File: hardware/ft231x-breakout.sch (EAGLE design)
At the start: 25 parts, among them Q1 2N7002PW, U1 FT231XS, X1 USB-MICROB

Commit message: Silkscreen fixes: no-silk headers, moved labels
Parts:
- JP1: device SparkFun-Connectors:M06SIP -> SparkFun-Connectors:M06SIP-NS
- JP10, JP11: device SparkFun-Connectors:M07 -> SparkFun-Connectors:M07NS
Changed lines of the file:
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@@
 <grid distance="0.1" unitdist="inch" unit="inch" style="lines" multiple="1" display="no" altdistance="0.01" altunitdist="inch" altunit="inch"/>
 <layers>
-<layer number="1" name="Top" color="4" fill="1" visible="no" active="no"/>
-<layer number="2" name="Route2" color="1" fill="3" visible="no" active="no"/>
-<layer number="3" name="Route3" color="4" fill="3" visible="no" active="no"/>
-<layer number="4" name="Route4" color="1" fill="4" visible="no" active="no"/>
-<layer number="5" name="Route5" color="4" fill="4" visible="no" active="no"/>
-<layer number="6" name="Route6" color="1" fill="8" visible="no" active="no"/>
-<layer number="7" name="Route7" color="4" fill="8" visible="no" active="no"/>
-<layer number="8" name="Route8" color="1" fill="2" visible="no" active="no"/>
-<layer number="9" name="Route9" color="4" fill="2" visible="no" active="no"/>
-<layer number="10" name="Route10" color="1" fill="7" visible="no" active="no"/>
-<layer number="11" name="Route11" color="4" fill="7" visible="no" active="no"/>
-<layer number="12" name="Route12" color="1" fill="5" visible="no" active="no"/>
-<layer number="13" name="Route13" color="4" fill="5" visible="no" active="no"/>
-<layer number="14" name="Route14" color="1" fill="6" visible="no" active="no"/>
-<layer number="15" name="Route15" color="4" fill="6" visible="no" active="no"/>
-<layer number="16" name="Bottom" color="1" fill="1" visible="no" active="no"/>
-<layer number="17" name="Pads" color="2" fill="1" visible="no" active="no"/>
-<layer number="18" name="Vias" color="2" fill="1" visible="no" active="no"/>
-<layer number="19" name="Unrouted" color="6" fill="1" visible="no" active="no"/>
-<layer number="20" name="Dimension" color="15" fill="1" visible="no" active="no"/>
-<layer number="21" name="tPlace" color="16" fill="1" visible="no" active="no"/>
-<layer number="22" name="bPlace" color="14" fill="1" visible="no" active="no"/>
-<layer number="23" name="tOrigins" color="15" fill="1" visible="no" active="no"/>
-<layer number="24" name="bOrigins" color="15" fill="1" visible="no" active="no"/>
-<layer number="25" name="tNames" color="7" fill="1" visible="no" active="no"/>
-<layer number="26" name="bNames" color="7" fill="1" visible="no" active="no"/>
-<layer number="27" name="tValues" color="7" fill="1" visible="no" active="no"/>
-<layer number="28" name="bValues" color="7" fill="1" visible="no" active="no"/>
+<layer number="1" name="Top" color="4" fill="1" visible="yes" active="no"/>
+<layer number="2" name="Route2" color="1" fill="3" visible="yes" active="no"/>
+<layer number="3" name="Route3" color="4" fill="3" visible="yes" active="no"/>
+<layer number="4" name="Route4" color="1" fill="4" visible="yes" active="no"/>
+<layer number="5" name="Route5" color="4" fill="4" visible="yes" active="no"/>
+<layer number="6" name="Route6" color="1" fill="8" visible="yes" active="no"/>
+<layer number="7" name="Route7" color="4" fill="8" visible="yes" active="no"/>
+<layer number="8" name="Route8" color="1" fill="2" visible="yes" active="no"/>
+<layer number="9" name="Route9" color="4" fill="2" visible="yes" active="no"/>
+<layer number="10" name="Route10" color="1" fill="7" visible="yes" active="no"/>
+<layer number="11" name="Route11" color="4" fill="7" visible="yes" active="no"/>
+<layer number="12" name="Route12" color="1" fill="5" visible="yes" active="no"/>
+<layer number="13" name="Route13" color="4" fill="5" visible="yes" active="no"/>
+<layer number="14" name="Route14" color="1" fill="6" visible="yes" active="no"/>
+<layer number="15" name="Route15" color="4" fill="6" visible="yes" active="no"/>
+<layer number="16" name="Bottom" color="1" fill="1" visible="yes" active="no"/>
+<layer number="17" name="Pads" color="2" fill="1" visible="yes" active="no"/>
+<layer number="18" name="Vias" color="2" fill="1" visible="yes" active="no"/>
+<layer number="19" name="Unrouted" color="6" fill="1" visible="yes" active="no"/>
+<layer number="20" name="Dimension" color="15" fill="1" visible="yes" active="no"/>
+<layer number="21" name="tPlace" color="16" fill="1" visible="yes" active="no"/>
+<layer number="22" name="bPlace" color="14" fill="1" visible="yes" active="no"/>
+<layer number="23" name="tOrigins" color="15" fill="1" visible="yes" active="no"/>
+<layer number="24" name="bOrigins" color="15" fill="1" visible="yes" active="no"/>
+<layer number="25" name="tNames" color="7" fill="1" visible="yes" active="no"/>
+<layer number="26" name="bNames" color="7" fill="1" visible="yes" active="no"/>
+<layer number="27" name="tValues" color="7" fill="1" visible="yes" active="no"/>
+<layer number="28" name="bValues" color="7" fill="1" visible="yes" active="no"/>
 <layer number="29" name="tStop" color="7" fill="3" visible="no" active="no"/>
 <layer number="30" name="bStop" color="7" fill="6" visible="no" active="no"/>
@@
 <layer number="35" name="tGlue" color="7" fill="4" visible="no" active="no"/>
 <layer number="36" name="bGlue" color="7" fill="5" visible="no" active="no"/>
-<layer number="37" name="tTest" color="7" fill="1" visible="no" active="no"/>
-<layer number="38" name="bTest" color="7" fill="1" visible="no" active="no"/>
+<layer number="37" name="tTest" color="7" fill="1" visible="yes" active="no"/>
+<layer number="38" name="bTest" color="7" fill="1" visible="yes" active="no"/>
 <layer number="39" name="tKeepout" color="4" fill="11" visible="no" active="no"/>
 <layer number="40" name="bKeepout" color="1" fill="11" visible="no" active="no"/>
@@
 <layer number="44" name="Drills" color="7" fill="1" visible="no" active="no"/>
 <layer number="45" name="Holes" color="7" fill="1" visible="no" active="no"/>
-<layer number="46" name="Milling" color="3" fill="1" visible="no" active="no"/>
-<layer number="47" name="Measures" color="7" fill="1" visible="no" active="no"/>
-<layer number="48" name="Document" color="7" fill="1" visible="no" active="no"/>
-<layer number="49" name="Reference" color="7" fill="1" visible="no" active="no"/>
-<layer number="50" name="dxf" color="7" fill="1" visible="no" active="no"/>
-<layer number="51" name="tDocu" color="6" fill="1" visible="no" active="no"/>
-<layer number="52" name="bDocu" color="7" fill="1" visible="no" active="no"/>
-<layer number="53" name="tGND_GNDA" color="7" fill="9" visible="no" active="no"/>
-<layer number="54" name="bGND_GNDA" color="1" fill="9" visible="no" active="no"/>
-<layer number="56" name="wert" color="7" fill="1" visible="no" active="no"/>
+<layer number="46" name="Milling" color="3" fill="1" visible="yes" active="no"/>
+<layer number="47" name="Measures" color="7" fill="1" visible="yes" active="no"/>
+<layer number="48" name="Document" color="7" fill="1" visible="yes" active="no"/>
+<layer number="49" name="Reference" color="7" fill="1" visible="yes" active="no"/>
+<layer number="50" name="dxf" color="7" fill="1" visible="yes" active="no"/>
+<layer number="51" name="tDocu" color="6" fill="1" visible="yes" active="no"/>
+<layer number="52" name="bDocu" color="7" fill="1" visible="yes" active="no"/>
+<layer number="53" name="tGND_GNDA" color="7" fill="9" visible="yes" active="no"/>
+<layer number="54" name="bGND_GNDA" color="1" fill="9" visible="yes" active="no"/>
+<layer number="56" name="wert" color="7" fill="1" visible="yes" active="no"/>
 <layer number="91" name="Nets" color="2" fill="1" visible="yes" active="yes"/>
 <layer number="92" name="Busses" color="1" fill="1" visible="yes" active="yes"/>
@@
 <part name="GND6" library="SparkFun-Aesthetics" deviceset="GND" device=""/>
 <part name="GND7" library="SparkFun-Aesthetics" deviceset="GND" device=""/>
-<part name="JP1" library="SparkFun-Connectors" deviceset="M06" device="SIP"/>
+<part name="JP1" library="SparkFun-Connectors" deviceset="M06" device="SIP-NS"/>
 <part name="GND8" library="SparkFun-Aesthetics" deviceset="GND" device=""/>
 <part name="SJ1" library="SparkFun-Passives" deviceset="SOLDERJUMPER_2WAY" device="S"/>
@@
 <part name="SJ2" library="SparkFun-Passives" deviceset="SOLDERJUMPER" device="TRACE" value="TXLED"/>
 <part name="SJ3" library="SparkFun-Passives" deviceset="SOLDERJUMPER" device="TRACE" value="RXLED"/>
-<part name="JP10" library="SparkFun-Connectors" deviceset="M07" device=""/>
-<part name="JP11" library="SparkFun-Connectors" deviceset="M07" device=""/>
+<part name="JP10" library="SparkFun-Connectors" deviceset="M07" device="NS"/>
+<part name="JP11" library="SparkFun-Connectors" deviceset="M07" device="NS"/>
 <part name="Q1" library="SparkFun-DiscreteSemi" deviceset="MOSFET-NCHANNEL" device="SOT323" value="2N7002PW"/>
 <part name="R5" library="SparkFun-Passives" deviceset="RESISTOR" device="0402-RES" value="10k"/>

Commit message: Added fiducials, minor silkscreen changes.
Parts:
- added JP3, JP4: FIDUCIALUFIDUCIAL, SparkFun-Aesthetics:FIDUCIALUFIDUCIAL
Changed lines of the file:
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@@
 <part name="JP2" library="SparkFun-Aesthetics" deviceset="LOGO-SFE" device="NW2"/>
 <part name="U$1" library="SparkFun-Aesthetics" deviceset="OSHW-LOGO" device="S"/>
+<part name="JP3" library="SparkFun-Aesthetics" deviceset="FIDUCIAL" device="UFIDUCIAL"/>
+<part name="JP4" library="SparkFun-Aesthetics" deviceset="FIDUCIAL" device="UFIDUCIAL"/>
 </parts>
 <sheets>
@@
 <instance part="JP2" gate="G$1" x="241.3" y="17.78"/>
 <instance part="U$1" gate="G$1" x="134.62" y="10.16"/>
+<instance part="JP3" gate="G$1" x="236.22" y="20.32"/>
+<instance part="JP4" gate="G$1" x="231.14" y="20.32"/>
 </instances>
 <busses>

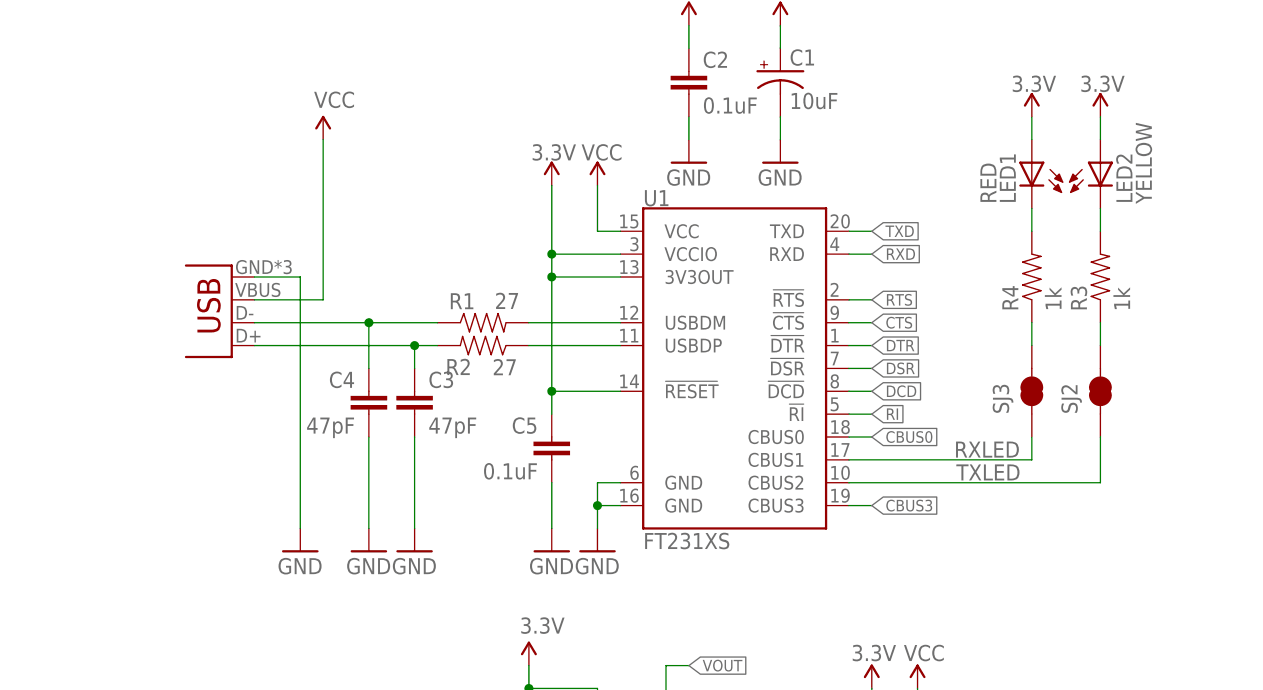
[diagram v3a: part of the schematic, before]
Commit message: Updated footprints, sch, microb
Updated to 0603 components
Updated to bossed microb
Trace reroutes
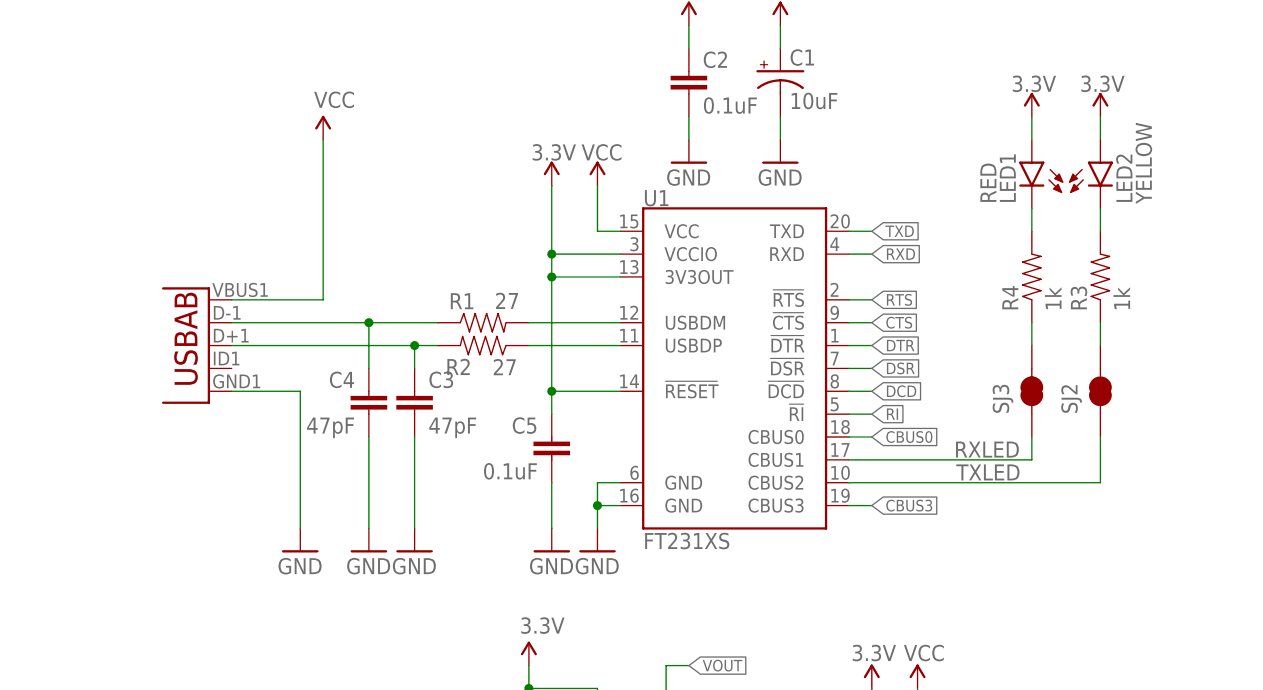
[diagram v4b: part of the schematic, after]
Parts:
- C2, C5: device SparkFun-Capacitors:CAP0402-CAP -> SparkFun-Capacitors:0.1UF-25V(+80/-20%)(0603)
- C3, C4: device SparkFun-Capacitors:CAP0402-CAP -> SparkFun-Capacitors:47PF-50V-5%(0603)
- LED2: device SparkFun-LED:LED0603 -> SparkFun-LED:LED-YELLOW0603
- R1, R2: device SparkFun-Resistors:RESISTOR0402-RES -> SparkFun-Resistors:RESISTOR0603-RES
- R3, R4: device SparkFun-Passives:RESISTOR0402-RES -> SparkFun-Resistors:1MOHM1/10W1%(0603)
- R5, R6: device SparkFun-Passives:RESISTOR0402-RES -> SparkFun-Resistors:10KOHM1/10W1%(0603)0603
- SJ3: device SparkFun-Passives:SOLDERJUMPERTRACE -> SparkFun-Passives:JUMPER-PAD-2-NC_BY_TRACE
- X1: value USB-MICROB -> (none); device SparkFun-Connectors:USB-MICROB -> SparkFun-Connectors:USB-ABCONN-11794

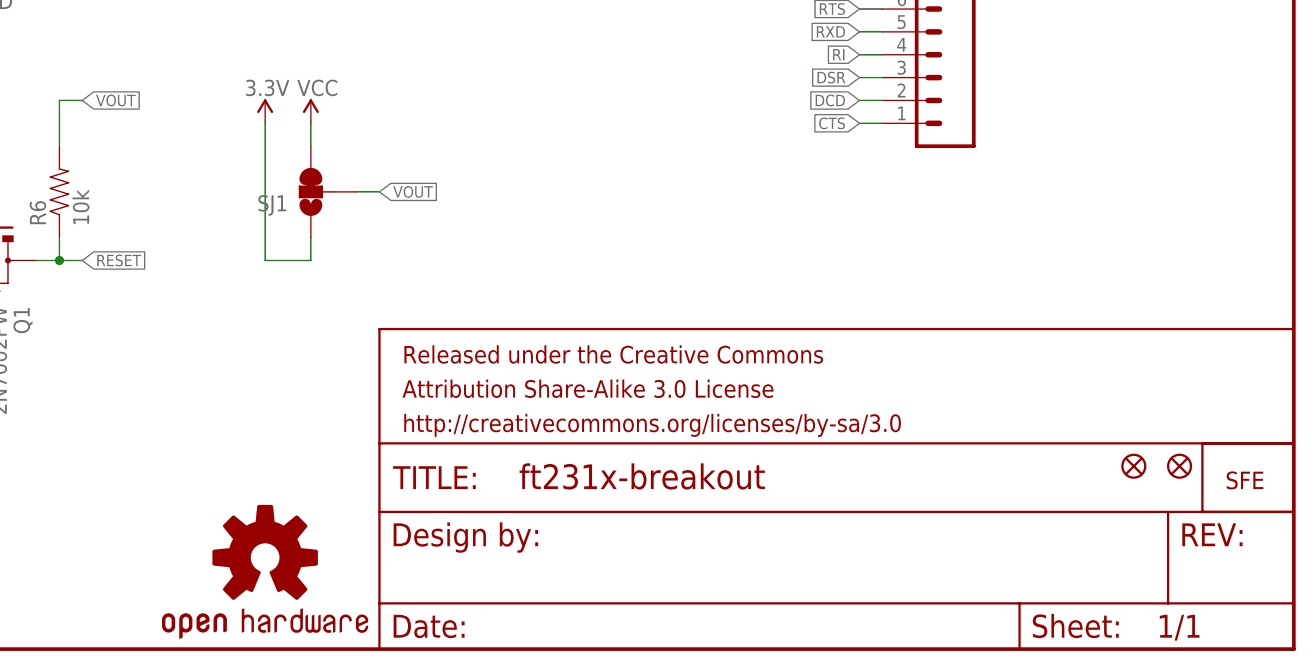
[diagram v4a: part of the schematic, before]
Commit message: Updated USB with Staking vias
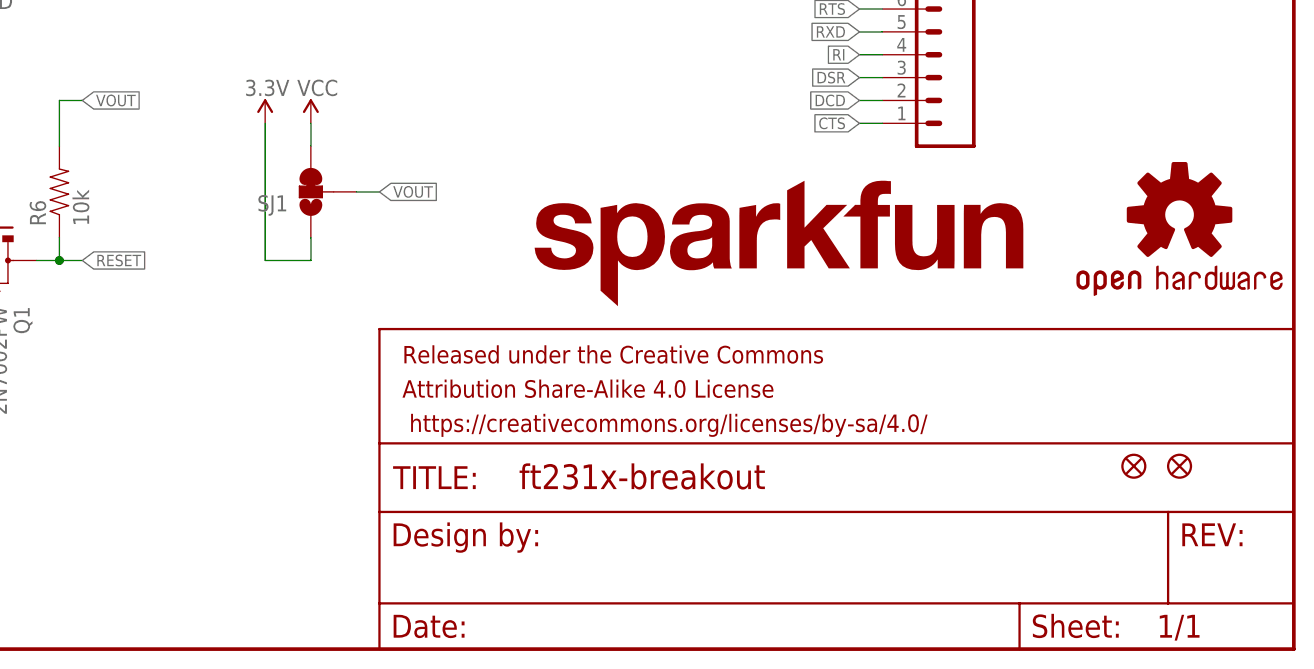
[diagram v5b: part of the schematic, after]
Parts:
- removed JP2: LOGO-SFENW2, SparkFun-Aesthetics:LOGO-SFENW2
- added LOGO1: SFE_LOGO_NAME.1_INCH, SparkFun-Aesthetics:SFE_LOGO_NAME.1_INCH
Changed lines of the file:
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@@
 <part name="R6" library="SparkFun-Resistors" deviceset="10KOHM1/10W1%(0603)" device="0603" value="10k"/>
 <part name="P+10" library="SparkFun-Aesthetics" deviceset="3.3V" device=""/>
-<part name="JP2" library="SparkFun-Aesthetics" deviceset="LOGO-SFE" device="NW2"/>
 <part name="U$1" library="SparkFun-Aesthetics" deviceset="OSHW-LOGO" device="S"/>
 <part name="JP3" library="SparkFun-Aesthetics" deviceset="FIDUCIAL" device="UFIDUCIAL"/>
 <part name="JP4" library="SparkFun-Aesthetics" deviceset="FIDUCIAL" device="UFIDUCIAL"/>
+<part name="LOGO1" library="SparkFun-Aesthetics" deviceset="SFE_LOGO_NAME" device=".1_INCH"/>
 </parts>
 <sheets>
@@
 <instance part="C5" gate="G$1" x="99.06" y="83.82" rot="MR0"/>
 <instance part="GND5" gate="1" x="99.06" y="73.66"/>
-<instance part="P+2" gate="1" x="104.14" y="114.3" smashed="yes">
+<instance part="P+2" gate="G$1" x="104.14" y="114.3" smashed="yes">
 <attribute name="VALUE" x="102.362" y="117.094" size="1.778" layer="96"/>
 </instance>
-<instance part="P+3" gate="1" x="114.3" y="132.08"/>
-<instance part="P+4" gate="1" x="124.46" y="132.08"/>
+<instance part="P+3" gate="G$1" x="114.3" y="132.08"/>
+<instance part="P+4" gate="G$1" x="124.46" y="132.08"/>
 <instance part="GND6" gate="1" x="114.3" y="116.84"/>
 <instance part="GND7" gate="1" x="124.46" y="116.84"/>
@@
 <attribute name="VALUE" x="96.774" y="117.094" size="1.778" layer="96"/>
 </instance>
-<instance part="P+6" gate="1" x="139.7" y="58.42" smashed="yes">
+<instance part="P+6" gate="G$1" x="139.7" y="58.42" smashed="yes">
 <attribute name="VALUE" x="138.176" y="61.468" size="1.778" layer="96"/>
 </instance>
@@
 <attribute name="VALUE" x="132.334" y="61.468" size="1.778" layer="96"/>
 </instance>
-<instance part="P+1" gate="1" x="73.66" y="119.38"/>
+<instance part="P+1" gate="G$1" x="73.66" y="119.38"/>
 <instance part="C1" gate="G$1" x="124.46" y="127"/>
 <instance part="LED1" gate="G$1" x="152.4" y="116.84" rot="MR0"/>
@@
 <instance part="R6" gate="G$1" x="111.76" y="50.8" rot="R90"/>
 <instance part="P+10" gate="G$1" x="96.52" y="60.96"/>
-<instance part="JP2" gate="G$1" x="241.3" y="17.78"/>
-<instance part="U$1" gate="G$1" x="134.62" y="10.16"/>
+<instance part="U$1" gate="G$1" x="236.22" y="48.26"/>
 <instance part="JP3" gate="G$1" x="236.22" y="20.32"/>
 <instance part="JP4" gate="G$1" x="231.14" y="20.32"/>
+<instance part="LOGO1" gate="G$1" x="162.56" y="38.1"/>
 </instances>
 <busses>
@@
 <wire x1="106.68" y1="109.22" x2="104.14" y2="109.22" width="0.1524" layer="91"/>
 <wire x1="104.14" y1="109.22" x2="104.14" y2="114.3" width="0.1524" layer="91"/>
-<pinref part="P+2" gate="1" pin="VCC"/>
+<pinref part="P+2" gate="G$1" pin="VCC"/>
 </segment>
 <segment>
 <pinref part="C2" gate="G$1" pin="1"/>
-<pinref part="P+3" gate="1" pin="VCC"/>
+<pinref part="P+3" gate="G$1" pin="VCC"/>
 <wire x1="114.3" y1="132.08" x2="114.3" y2="129.54" width="0.1524" layer="91"/>
 </segment>
 <segment>
 <pinref part="SJ1" gate="G$1" pin="3"/>
-<pinref part="P+6" gate="1" pin="VCC"/>
+<pinref part="P+6" gate="G$1" pin="VCC"/>
 <wire x1="139.7" y1="58.42" x2="139.7" y2="55.88" width="0.1524" layer="91"/>
 </segment>
@@
 <pinref part="X1" gate="G$1" pin="VBUS"/>
 <wire x1="63.5" y1="101.6" x2="73.66" y2="101.6" width="0.1524" layer="91"/>
-<pinref part="P+1" gate="1" pin="VCC"/>
+<pinref part="P+1" gate="G$1" pin="VCC"/>
 <wire x1="73.66" y1="101.6" x2="73.66" y2="119.38" width="0.1524" layer="91"/>
 </segment>
@@
 <segment>
 <pinref part="C1" gate="G$1" pin="+"/>
-<pinref part="P+4" gate="1" pin="VCC"/>
+<pinref part="P+4" gate="G$1" pin="VCC"/>
 <wire x1="124.46" y1="129.54" x2="124.46" y2="132.08" width="0.1524" layer="91"/>
 </segment>

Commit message: Initial QC CL, Updated Parts, Fixed SCH.
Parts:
- removed LED1: RED, SparkFun-LED:LED0603
- removed LED2: YELLOW, SparkFun-LED:LED-YELLOW0603
- added D1: RED, SparkFun-LED:LED-RED0603
- added D2: YELLOW, SparkFun-LED:LED-YELLOW0603
- C1: device SparkFun-Passives:CAP_POL1206 -> SparkFun-Capacitors:10UF-16V-10%(TANT)
- Q1: device SparkFun-DiscreteSemi:MOSFET-NCHANNELSOT323 -> SparkFun-DiscreteSemi:MOSFET-NCHANNEL2N7002PW
- R1, R2: device SparkFun-Resistors:RESISTOR0603-RES -> SparkFun-Resistors:27OHM1/10W1%(0603)0603-RES
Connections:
- net 3.3V: now also D1.A, D2.A; no longer LED1.A, LED2.A
- net N$5: now also D2.C; no longer LED2.C
- net N$6: now also D1.C; no longer LED1.C
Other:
- note added: "Jim Lindblom"
- note added: "Revised by: Patrick Alberts"
- note added: "V10"
- moved on the sheet: C1, C2, C3, C4, C5, JP1, JP10, JP11, Q1, R1, R2, R3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
